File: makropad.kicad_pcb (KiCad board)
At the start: 2 copper layers, 33 parts, among them J1 OLED_DISPLAY, SW1 SW_Push_45deg, SW10 SW_Push_45deg, SW11 RotaryEncoder_Switch, SW12 RotaryEncoder_Switch, SW2 SW_Push_45deg, SW3 SW_Push_45deg, SW4 SW_Push_45deg, SW5 SW_Push_45deg, SW6 SW_Push_45deg, SW7 SW_Push_45deg, SW8 SW_Push_45deg, SW9 SW_Push_45deg, U1 PCF8574A, U2 MOUDLE-SEEEDUINO-XIAO

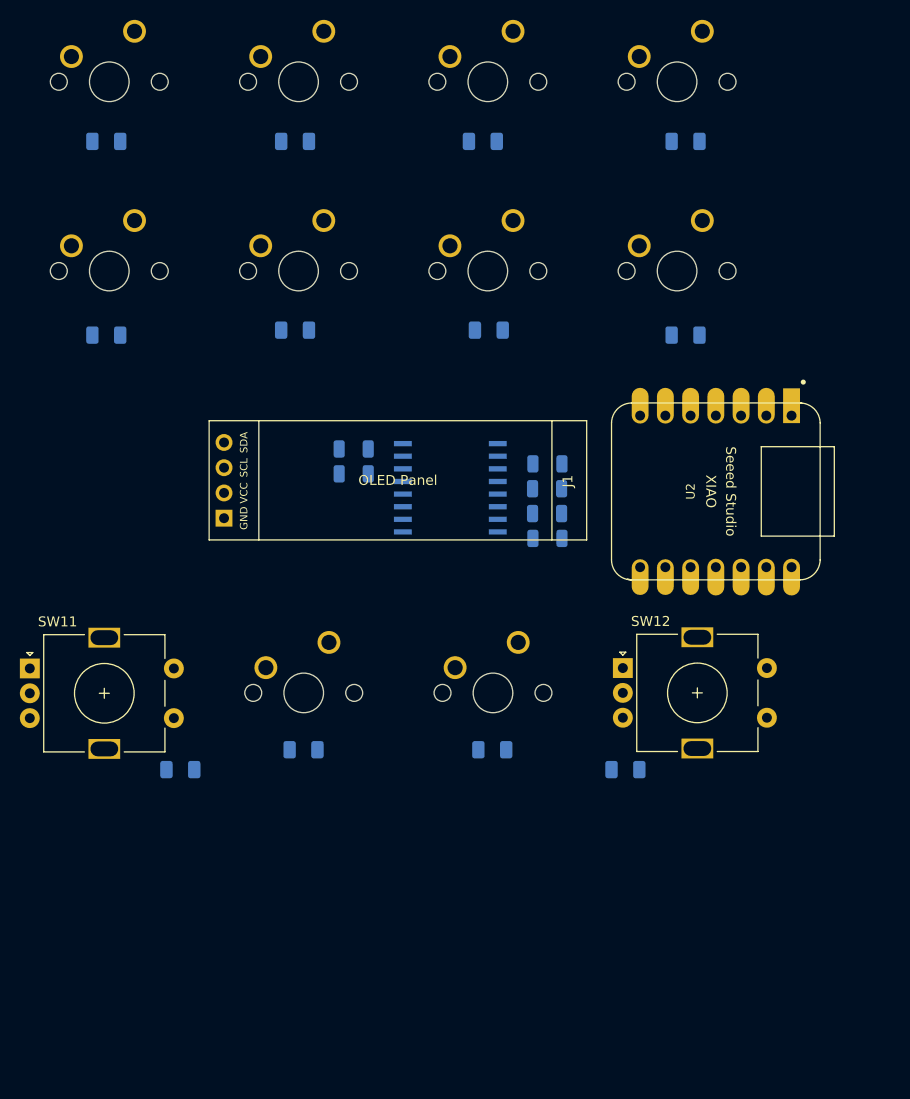
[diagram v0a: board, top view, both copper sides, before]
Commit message: feat: finish pcb placement
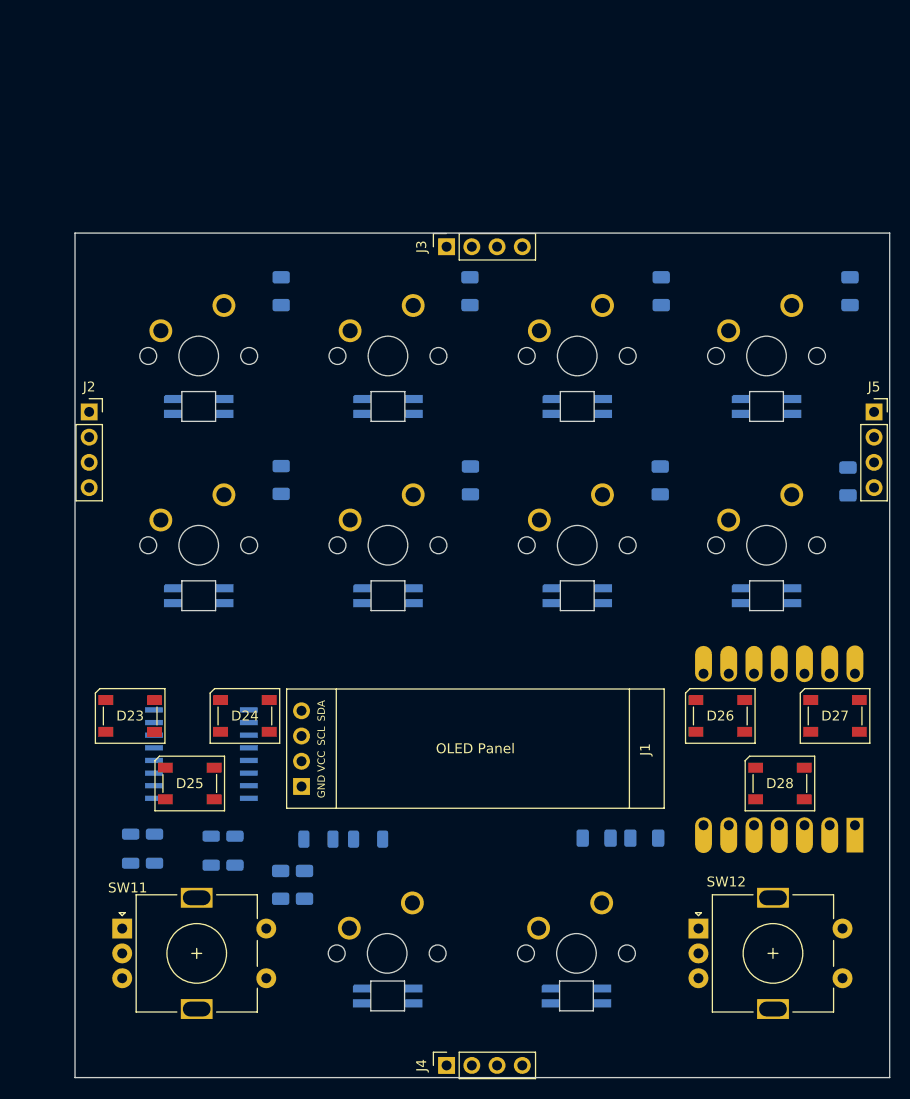
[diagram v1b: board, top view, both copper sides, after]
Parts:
- added D13: SK6812, Components:SK6812MINI-E, B.Cu at (124.0, 60.5)
- added D14: SK6812, Components:SK6812MINI-E, B.Cu at (143.0, 60.5)
- added D15: SK6812, Components:SK6812MINI-E, B.Cu at (162.1, 60.5)
- added D16: SK6812, Components:SK6812MINI-E, B.Cu at (181.1, 60.5)
- added D17: SK6812, Components:SK6812MINI-E, B.Cu at (124.0, 79.5)
- added D18: SK6812, Components:SK6812MINI-E, B.Cu at (143.0, 79.5)
- added D19: SK6812, Components:SK6812MINI-E, B.Cu at (162.1, 79.5)
- added D20: SK6812, Components:SK6812MINI-E, B.Cu at (181.1, 79.5)
- added D21: SK6812, Components:SK6812MINI-E, B.Cu at (143.0, 119.8)
- added D22: SK6812, Components:SK6812MINI-E, B.Cu at (162.0, 119.8)
- added D23: SK6812, LED_SMD:LED_SK6812_PLCC4_5.0x5.0mm_P3.2mm, F.Cu at (117.0, 91.6)
- added D24: SK6812, LED_SMD:LED_SK6812_PLCC4_5.0x5.0mm_P3.2mm, F.Cu at (128.6, 91.6)
- added D25: SK6812, LED_SMD:LED_SK6812_PLCC4_5.0x5.0mm_P3.2mm, F.Cu at (123.0, 98.4)
- added D26: SK6812, LED_SMD:LED_SK6812_PLCC4_5.0x5.0mm_P3.2mm, F.Cu at (176.4, 91.6)
- added D27: SK6812, LED_SMD:LED_SK6812_PLCC4_5.0x5.0mm_P3.2mm, F.Cu at (188.0, 91.6)
- added D28: SK6812, LED_SMD:LED_SK6812_PLCC4_5.0x5.0mm_P3.2mm, F.Cu at (182.4, 98.4)
- added J2: Conn_01x04, Connector_PinSocket_2.54mm:PinSocket_1x04_P2.54mm_Vertical, F.Cu at (112.9, 61.0)
- added J3: Conn_01x04, Connector_PinSocket_2.54mm:PinSocket_1x04_P2.54mm_Vertical, F.Cu at (148.9, 44.4)
- added J4: Conn_01x04, Connector_PinSocket_2.54mm:PinSocket_1x04_P2.54mm_Vertical, F.Cu at (148.9, 126.8)
- added J5: Conn_01x04, Connector_PinSocket_2.54mm:PinSocket_1x04_P2.54mm_Vertical, F.Cu at (191.9, 61.0)
- U2: moved to B.Cu
- moved R6 57.1 mm to (117.1, 105.0), turned to 90 degrees
- moved R5 53.6 mm to (119.5, 105.0), turned to 90 degrees
- moved R4 47.9 mm to (125.2, 105.2), turned to 90 degrees
- moved R3 44.5 mm to (127.6, 105.2), turned to 90 degrees
- moved R1 39.3 mm to (141.0, 104.0)
- moved R2 36.9 mm to (136.0, 104.0), turned to 0 degrees
- moved U1 36.7 mm to (124.2, 95.4), turned to 0 degrees
- moved SW5 29.0 mm to (124.0, 74.4)
- moved SW6 29.0 mm to (143.0, 74.4)
- moved SW7 29.0 mm to (162.1, 74.4)
- moved SW8 29.0 mm to (181.1, 74.4)
- moved SW1 29.0 mm to (124.0, 55.4)
- moved SW2 29.0 mm to (143.0, 55.4)
- moved SW3 29.0 mm to (162.1, 55.4)
- moved SW4 29.0 mm to (181.1, 55.4)
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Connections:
- U2 pad 7: unconnected-(U2-PB08_A6_D6_TX-Pad7) -> RGB
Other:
- board outline added: 82 x 85 mm

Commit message: feat: fully route pcb
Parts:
- moved U2 1.00 mm to (183.4, 95.0)
- moved J4 0.20 mm to (148.9, 126.6)
- moved J3 0.10 mm to (148.9, 44.5)
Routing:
- net GND: track 0.00 -> 428.3 mm, vias 0 -> 8
- net VCC: track 0.00 -> 384.1 mm, vias 0 -> 9
- net I2C_SCL: track 0.00 -> 227.6 mm, vias 0 -> 2
- net I2C_SDA: track 0.00 -> 219.1 mm, vias 0 -> 2
- net COL0: track 0.00 -> 127.3 mm, vias 0 -> 1
- net COL3: track 0.00 -> 122.0 mm, vias 0 -> 1
- net COL1: track 0.00 -> 110.8 mm, vias 0 -> 1
- net RGB: track 0.00 -> 104.0 mm, vias 0 -> 1
- net ROW0: track 0.00 -> 102.9 mm, vias 0 -> 1
- net COL2: track 0.00 -> 88.9 mm, vias 0 -> 1
- net ROW1: track 0.00 -> 81.1 mm, vias 0 -> 1
- net Net-(D20-DOUT): track 0.00 -> 78.4 mm, vias 0 -> 2
- net Net-(D16-DOUT): track 0.00 -> 78.3 mm, vias 0 -> 2
- net ENC_2_B: track 0.00 -> 73.1 mm, vias 0 -> 2
- net ENC_2_A: track 0.00 -> 69.2 mm
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
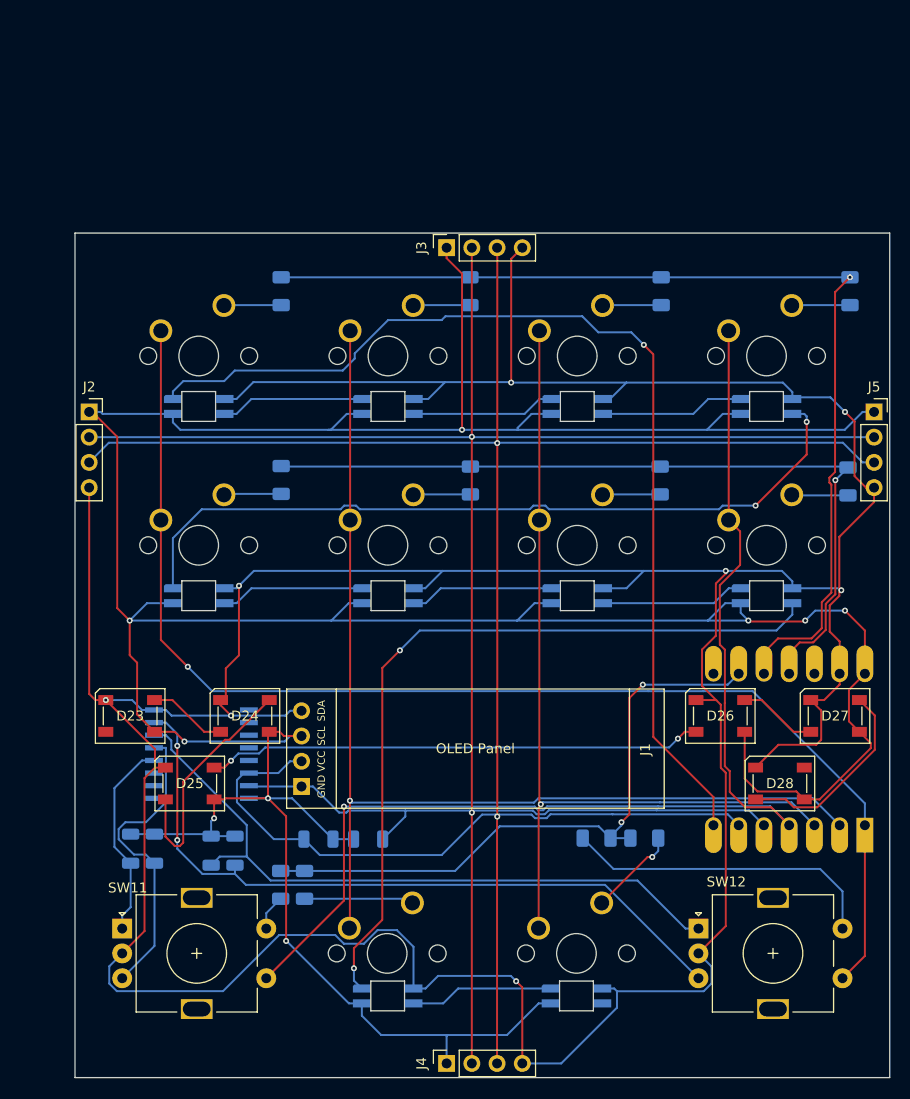
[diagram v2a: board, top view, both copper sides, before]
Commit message: feat: add 3d renders
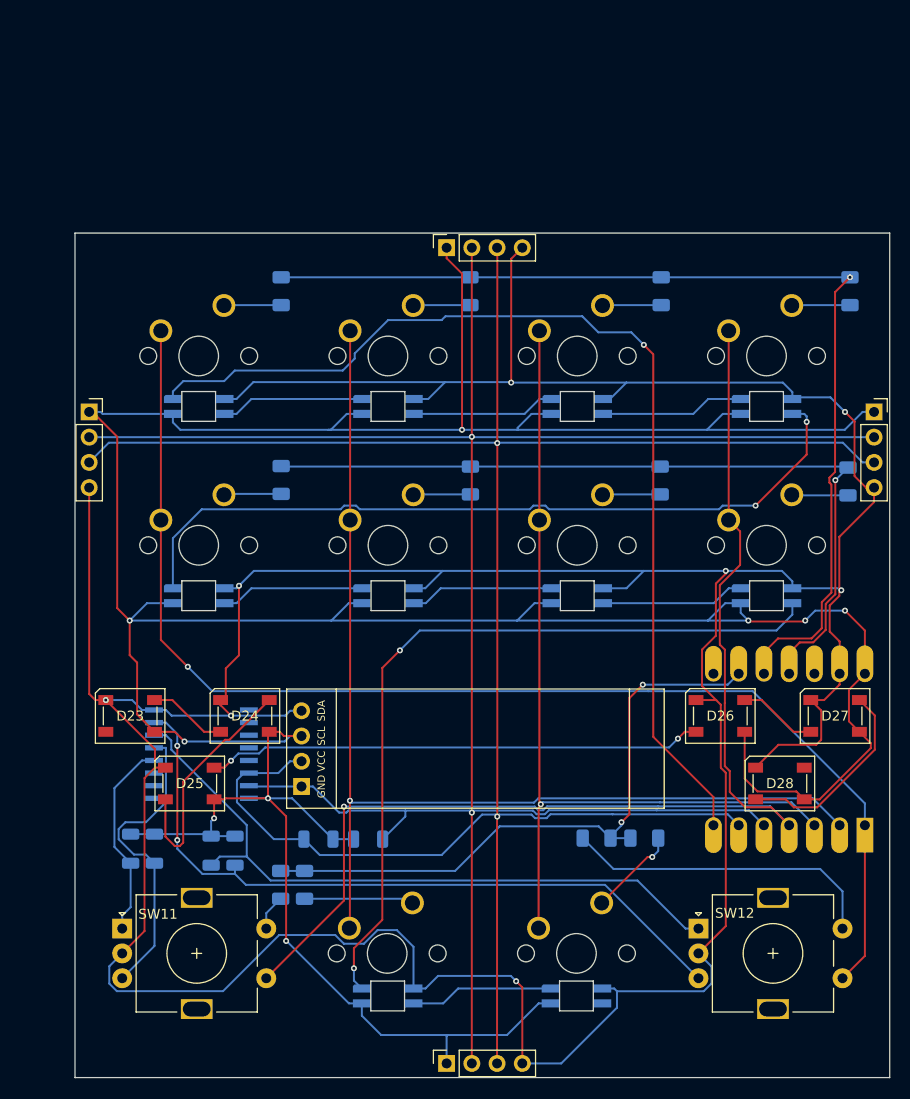
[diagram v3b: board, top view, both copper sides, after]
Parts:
- J2, J3, J4, J5: footprint Connector_PinSocket_2.54mm:PinSocket_1x04_P2.54mm_Vertical -> Components:4pin
- SW11, SW12: footprint Rotary_Encoder:RotaryEncoder_Alps_EC11E-Switch_Vertical_H20mm -> Components:encoder
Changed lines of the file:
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@@
 			(pintype "passive")
 		)
+		(model "${KIPRJMOD}/Components/CherryMX.wrl"
+			(offset
+				(xyz 7.5 7.5 6)
+			)
+			(scale
+				(xyz 0.4 0.4 0.4)
+			)
+			(rotate
+				(xyz -90 0 180)
+			)
+		)
 	)
 	(footprint "Components:MX-Solderable-1U"
@@
 			(pintype "passive")
 		)
+		(model "${KIPRJMOD}/Components/CherryMX.wrl"
+			(offset
+				(xyz 7.5 7.5 6)
+			)
+			(scale
+				(xyz 0.4 0.4 0.4)
+			)
+			(rotate
+				(xyz -90 0 180)
+			)
+		)
 	)
 	(footprint "Components:MX-Solderable-1U"
@@
 			(pintype "passive")
 		)
+		(model "${KIPRJMOD}/Components/CherryMX.wrl"
+			(offset
+				(xyz 7.5 7.5 6)
+			)
+			(scale
+				(xyz 0.4 0.4 0.4)
+			)
+			(rotate
+				(xyz -90 0 180)
+			)
+		)
 	)
-	(footprint "Connector_PinSocket_2.54mm:PinSocket_1x04_P2.54mm_Vertical"
+	(footprint "Components:4pin"
 		(layer "F.Cu")
 		(at 191.925 61)
@@
 		(tags "Through hole socket strip THT 1x04 2.54mm single row")
 		(property "Reference" "J5"
-			(at 0 -2.52 0)
+			(at 0 -2.77 0)
 			(layer "F.SilkS")
+			(hide yes)
 			(effects
 				(font
@@
 		)
 		(property "Value" "Conn_01x04"
-			(at -0.025 10.2 0)
+			(at 0 10.39 0)
 			(layer "F.Fab")
 			(effects
@@
 			)
 		)
-		(property "Footprint" "Connector_PinSocket_2.54mm:PinSocket_1x04_P2.54mm_Vertical"
+		(property "Footprint" "Components:4pin"
 			(at 0 0 0)
 			(unlocked yes)
@@
 		)
 		(model "${KICAD8_3DMODEL_DIR}/Connector_PinSocket_2.54mm.3dshapes/PinSocket_1x04_P2.54mm_Vertical.wrl"
+			(hide yes)
 			(offset
 				(xyz 0 0 0)
@@
 			(at 1.9 5.91 90)
 			(layer "F.SilkS")
+			(hide yes)
 			(effects
 				(font
@@
 			(at 18.5 14 0)
 			(layer "F.Fab")
+			(hide yes)
 			(effects
 				(font
@@
 			(layer "F.CrtYd")
 		)
-		(fp_text user "OLED Panel"
-			(at 19 6 0)
+		(fp_text user "VCC"
+			(at 34.5 4.73 90)
 			(layer "F.SilkS")
 			(effects
 				(font
-					(size 1 1)
+					(size 0.75 0.75)
 					(thickness 0.15)
 				)
@@
 			)
 		)
-		(fp_text user "VCC"
-			(at 34.5 4.73 90)
-			(layer "F.SilkS")
-			(effects
-				(font
-					(size 0.75 0.75)
-					(thickness 0.15)
-				)
-			)
-		)
 		(pad "1" thru_hole rect
 			(at 36.5 2.19 180)
@@
 			(pintype "passive")
 		)
+		(model "${KIPRJMOD}/Components/OLED_0.91_128x32.stp"
+			(offset
+				(xyz 19 -6 3)
+			)
+			(scale
+				(xyz 1 1 1)
+			)
+			(rotate
+				(xyz 0 0 180)
+			)
+		)
 	)
 	(footprint "LED_SMD:LED_SK6812_PLCC4_5.0x5.0mm_P3.2mm"
@@
 		)
 	)
-	(footprint "Connector_PinSocket_2.54mm:PinSocket_1x04_P2.54mm_Vertical"
+	(footprint "Components:4pin"
 		(layer "F.Cu")
 		(at 112.925 61)
@@
 		(tags "Through hole socket strip THT 1x04 2.54mm single row")
 		(property "Reference" "J2"
-			(at 0 -2.52 0)
+			(at 0 -2.77 0)
 			(layer "F.SilkS")
+			(hide yes)
 			(effects
 				(font
@@
 			)
 		)
-		(property "Footprint" "Connector_PinSocket_2.54mm:PinSocket_1x04_P2.54mm_Vertical"
+		(property "Footprint" "Components:4pin"
 			(at 0 0 0)
 			(unlocked yes)
@@
 		)
 		(model "${KICAD8_3DMODEL_DIR}/Connector_PinSocket_2.54mm.3dshapes/PinSocket_1x04_P2.54mm_Vertical.wrl"
+			(hide yes)
 			(offset
 				(xyz 0 0 0)
@@
 		)
 	)
-	(footprint "Rotary_Encoder:RotaryEncoder_Alps_EC11E-Switch_Vertical_H20mm"
+	(footprint "Components:encoder"
 		(layer "F.Cu")
 		(at 174.25 113)
@@
 		(tags "rotary encoder")
 		(property "Reference" "SW12"
-			(at 2.8 -4.7 0)
+			(at 3.65 -1.55 0)
 			(layer "F.SilkS")
 			(effects
@@
 			)
 		)
-		(property "Footprint" "Rotary_Encoder:RotaryEncoder_Alps_EC11E-Switch_Vertical_H20mm"
+		(property "Footprint" "Components:encoder"
 			(at 0 0 0)
 			(unlocked yes)
@@
 			(pintype "passive")
 		)
-		(model "${KICAD8_3DMODEL_DIR}/Rotary_Encoder.3dshapes/RotaryEncoder_Alps_EC11E-Switch_Vertical_H20mm.wrl"
+		(model "${KIPRJMOD}/Components/EC11_Rotary_Encoder_Switched.wrl"
 			(offset
-				(xyz 0 0 0)
+				(xyz 7.5 -2.5 0)
 			)
 			(scale
-				(xyz 1 1 1)
+				(xyz 1 0.95 1)
 			)
 			(rotate
-				(xyz 0 0 0)
+				(xyz 0 0 90)
 			)
 		)
@@
 			(pintype "passive")
 		)
+		(model "${KIPRJMOD}/Components/CherryMX.wrl"
+			(offset
+				(xyz 7.5 7.5 6)
+			)
+			(scale
+				(xyz 0.4 0.4 0.4)
+			)
+			(rotate
+				(xyz -90 0 180)
+			)
+		)
 	)
-	(footprint "Connector_PinSocket_2.54mm:PinSocket_1x04_P2.54mm_Vertical"
+	(footprint "Components:4pin"
 		(layer "F.Cu")
 		(at 148.9 44.475 90)
@@
 		(tags "Through hole socket strip THT 1x04 2.54mm single row")
 		(property "Reference" "J3"
-			(at 0 -2.52 90)
+			(at 0 -2.77 90)
 			(layer "F.SilkS")
+			(hide yes)
 			(effects
 				(font
@@
 			)
 		)
-		(property "Footprint" "Connector_PinSocket_2.54mm:PinSocket_1x04_P2.54mm_Vertical"
+		(property "Footprint" "Components:4pin"
 			(at 0 0 90)
 			(unlocked yes)
@@
 		)
 		(fp_text user "${REFERENCE}"
-			(at 0 3.81 0)
+			(at 0 3.81 180)
 			(layer "F.Fab")
 			(effects
@@
 		)
 		(model "${KICAD8_3DMODEL_DIR}/Connector_PinSocket_2.54mm.3dshapes/PinSocket_1x04_P2.54mm_Vertical.wrl"
+			(hide yes)
 			(offset
 				(xyz 0 0 0)
@@
 			(pintype "passive")
 		)
+		(model "${KIPRJMOD}/Components/CherryMX.wrl"
+			(offset
+				(xyz 7.5 7.5 6)
+			)
+			(scale
+				(xyz 0.4 0.4 0.4)
+			)
+			(rotate
+				(xyz -90 0 180)
+			)
+		)
 	)
 	(footprint "Components:MX-Solderable-1U"
@@
 			(pintype "passive")
 		)
+		(model "${KIPRJMOD}/Components/CherryMX.wrl"
+			(offset
+				(xyz 7.5 7.5 6)
+			)
+			(scale
+				(xyz 0.4 0.4 0.4)
+			)
+			(rotate
+				(xyz -90 0 180)
+			)
+		)
 	)
-	(footprint "Rotary_Encoder:RotaryEncoder_Alps_EC11E-Switch_Vertical_H20mm"
+	(footprint "Components:encoder"
 		(layer "F.Cu")
 		(at 116.25 113)
@@
 		(tags "rotary encoder")
 		(property "Reference" "SW11"
-			(at 0.55 -4.1 0)
+			(at 3.6 -1.45 0)
 			(layer "F.SilkS")
 			(effects
@@
 			)
 		)
-		(property "Footprint" "Rotary_Encoder:RotaryEncoder_Alps_EC11E-Switch_Vertical_H20mm"
+		(property "Footprint" "Components:encoder"
 			(at 0 0 0)
 			(unlocked yes)
@@
 			(pintype "passive")
 		)
-		(model "${KICAD8_3DMODEL_DIR}/Rotary_Encoder.3dshapes/RotaryEncoder_Alps_EC11E-Switch_Vertical_H20mm.wrl"
+		(model "${KIPRJMOD}/Components/EC11_Rotary_Encoder_Switched.wrl"
 			(offset
-				(xyz 0 0 0)
+				(xyz 7.5 -2.5 0)
 			)
 			(scale
-				(xyz 1 1 1)
+				(xyz 1 0.95 1)
 			)
 			(rotate
-				(xyz 0 0 0)
+				(xyz 0 0 90)
 			)
 		)
@@
 			(pintype "passive")
 		)
+		(model "${KIPRJMOD}/Components/CherryMX.wrl"
+			(offset
+				(xyz 7.5 7.5 6)
+			)
+			(scale
+				(xyz 0.4 0.4 0.4)
+			)
+			(rotate
+				(xyz -90 0 180)
+			)
+		)
 	)
-	(footprint "Connector_PinSocket_2.54mm:PinSocket_1x04_P2.54mm_Vertical"
+	(footprint "Components:4pin"
 		(layer "F.Cu")
 		(at 148.9 126.575 90)
@@
 		(tags "Through hole socket strip THT 1x04 2.54mm single row")
 		(property "Reference" "J4"
-			(at 0 -2.52 90)
+			(at 0 -2.77 90)
 			(layer "F.SilkS")
+			(hide yes)
 			(effects
 				(font
@@
 		)
 		(property "Value" "Conn_01x04"
-			(at 0.4 10.08 90)
+			(at 0 10.39 90)
 			(layer "F.Fab")
 			(effects
@@
 			)
 		)
-		(property "Footprint" "Connector_PinSocket_2.54mm:PinSocket_1x04_P2.54mm_Vertical"
+		(property "Footprint" "Components:4pin"
 			(at 0 0 90)
 			(unlocked yes)
@@
 		)
 		(fp_text user "${REFERENCE}"
-			(at 0 3.81 0)
+			(at 0 3.81 180)
 			(layer "F.Fab")
 			(effects
@@
 		)
 		(model "${KICAD8_3DMODEL_DIR}/Connector_PinSocket_2.54mm.3dshapes/PinSocket_1x04_P2.54mm_Vertical.wrl"
+			(hide yes)
 			(offset
 				(xyz 0 0 0)
@@
 			(pintype "passive")
 		)
+		(model "${KIPRJMOD}/Components/CherryMX.wrl"
+			(offset
+				(xyz 7.5 7.5 6)
+			)
+			(scale
+				(xyz 0.4 0.4 0.4)
+			)
+			(rotate
+				(xyz -90 0 180)
+			)
+		)
 	)
 	(footprint "Components:MX-Solderable-1U"
@@
 			(pintype "passive")
 		)
+		(model "${KIPRJMOD}/Components/CherryMX.wrl"
+			(offset
+				(xyz 7.5 7.5 6)
+			)
+			(scale
+				(xyz 0.4 0.4 0.4)
+			)
+			(rotate
+				(xyz -90 0 180)
+			)
+		)
 	)
 	(footprint "Components:MX-Solderable-1U"
@@
 			(pintype "passive")
 		)
+		(model "${KIPRJMOD}/Components/CherryMX.wrl"
+			(offset
+				(xyz 7.5 7.5 6)
+			)
+			(scale
+				(xyz 0.4 0.4 0.4)
+			)
+			(rotate
+				(xyz -90 0 180)
+			)
+		)
 	)
